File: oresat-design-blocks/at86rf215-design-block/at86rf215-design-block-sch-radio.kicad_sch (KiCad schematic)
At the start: 45 parts, among them J1 SMA, J10 Conn_01x08, J11 Conn_01x05, J12 Conn_01x08, J2 USB4105-GF-A, J3 Conn_01x06, J6 Conn_01x06, J9 Screw_Terminal_01x02, SW1 RESET, U1 AT86RF215, U2 LP2985AIM5-1.8_NOPB, X1 TXETALSANF-26.000000

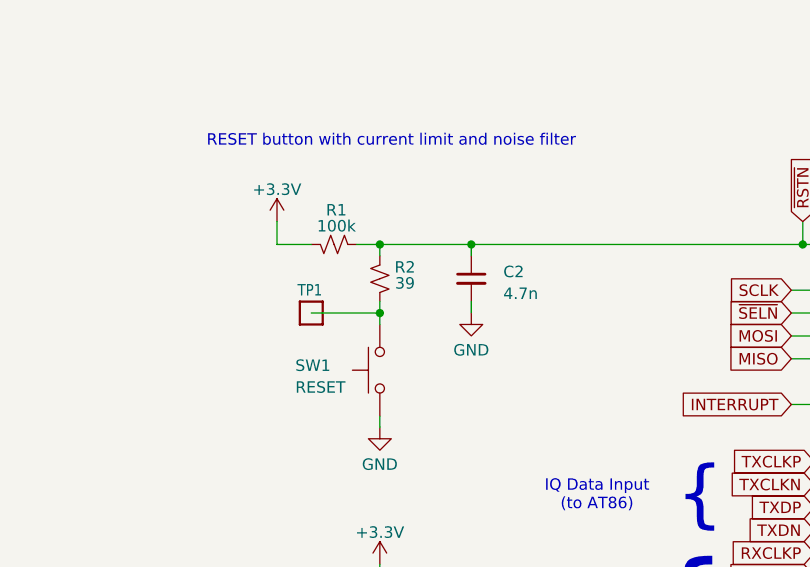
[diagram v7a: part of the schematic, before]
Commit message: Final polish on AT86 board
Changed differential lines to 100 ohms, uncovered all RF traces with solder mask, switch all caps and resistors to common footprint, added most BOM parts, moved RF components to not add stubs, fixed DRC violations and cleaned up silk screen.
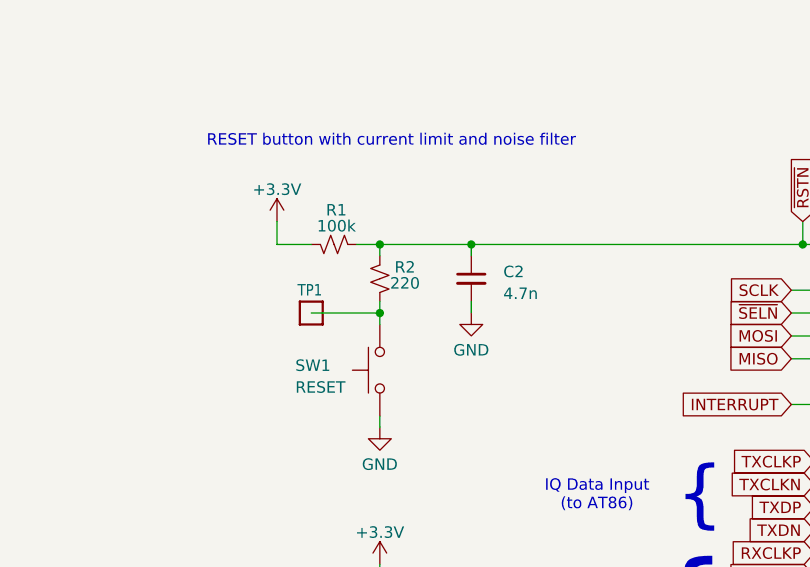
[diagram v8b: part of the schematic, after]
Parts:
- C14, C15, C16, C2, C4: footprint Capacitor_SMD:C_0603_1608Metric -> oresat-passives:0603-C-NOSILK
- C3: footprint Capacitor_SMD:C_0402_1005Metric -> oresat-passives:0603-C-NOSILK
- J10, J12: DIS (none) -> Digikey; DPN (none) -> SAM1029-08-ND; MFR (none) -> Samtec Inc.; MPN (none) -> TSW-108-07-G-S
- J11: DIS (none) -> Digikey; DPN (none) -> SAM1029-05-ND; MFR (none) -> Samtec Inc.; MPN (none) -> TSW-105-07-G-S
- J3, J6: DIS (none) -> Digikey; DPN (none) -> SAM1029-06-ND; MFR (none) -> Samtec Inc.; MPN (none) -> TSW-106-07-G-S
- R1, R4, R7: footprint Resistor_SMD:R_0603_1608Metric -> oresat-passives:0603-C-NOSILK
- R2: value 39 -> 220; footprint Resistor_SMD:R_0603_1608Metric -> oresat-passives:0603-C-NOSILK; DIS (none) -> DigiKey; DPN (none) -> RMCF0603FT200RCT-ND; MFR (none) -> Stackpole Electronics Inc; MPN (none) -> RMCF0603FT200R
- R3: footprint Resistor_SMD:R_0603_1608Metric -> oresat-passives:0603-C-NOSILK; DIS (none) -> DigiKey; DPN (none) -> RMCF0603FT200RCT-ND; MFR (none) -> Stackpole Electronics Inc; MPN (none) -> RMCF0603FT200R
- U1: DIS (none) -> DigiKey; DPN (none) -> AT86RF215-ZURCT-ND; MFR (none) -> Microchip; MPN (none) -> AT86RF215-ZUR
- U2: DIS (none) -> DigiKey
